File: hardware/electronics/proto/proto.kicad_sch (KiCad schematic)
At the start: 49 parts, among them J1 Conn_01x08_Female, U1 ADS131M06, U2 AP131-30

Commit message: Switch strain gauge footprints
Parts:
- R1, R10, R11, R12, R2, R3, R4, R5, R6, R7, R8, R9: value 1k -> 350; footprint Resistor_SMD:R_2512_6332Metric_Pad1.40x3.35mm_HandSolder -> proto:StrainGauge_BF350-3AA
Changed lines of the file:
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@@
       (effects (font (size 1.27 1.27)) (justify left))
     )
-    (property "Value" "1k" (id 1) (at 74.168 95.6822 0)
-      (effects (font (size 1.27 1.27)) (justify left))
-    )
-    (property "Footprint" "Resistor_SMD:R_2512_6332Metric_Pad1.40x3.35mm_HandSolder" (id 2) (at 70.612 93.98 90)
+    (property "Value" "350" (id 1) (at 74.168 95.6822 0)
+      (effects (font (size 1.27 1.27)) (justify left))
+    )
+    (property "Footprint" "proto:StrainGauge_BF350-3AA" (id 2) (at 70.612 93.98 90)
       (effects (font (size 1.27 1.27)) hide)
     )
@@
       (effects (font (size 1.27 1.27)) (justify left))
     )
-    (property "Value" "1k" (id 1) (at 61.468 85.5222 0)
-      (effects (font (size 1.27 1.27)) (justify left))
-    )
-    (property "Footprint" "Resistor_SMD:R_2512_6332Metric_Pad1.40x3.35mm_HandSolder" (id 2) (at 57.912 83.82 90)
+    (property "Value" "350" (id 1) (at 61.468 85.5222 0)
+      (effects (font (size 1.27 1.27)) (justify left))
+    )
+    (property "Footprint" "proto:StrainGauge_BF350-3AA" (id 2) (at 57.912 83.82 90)
       (effects (font (size 1.27 1.27)) hide)
     )
@@
       (effects (font (size 1.27 1.27)) (justify left))
     )
-    (property "Value" "1k" (id 1) (at 61.468 95.6822 0)
-      (effects (font (size 1.27 1.27)) (justify left))
-    )
-    (property "Footprint" "Resistor_SMD:R_2512_6332Metric_Pad1.40x3.35mm_HandSolder" (id 2) (at 57.912 93.98 90)
+    (property "Value" "350" (id 1) (at 61.468 95.6822 0)
+      (effects (font (size 1.27 1.27)) (justify left))
+    )
+    (property "Footprint" "proto:StrainGauge_BF350-3AA" (id 2) (at 57.912 93.98 90)
       (effects (font (size 1.27 1.27)) hide)
     )
@@
       (effects (font (size 1.27 1.27)) (justify left))
     )
-    (property "Value" "1k" (id 1) (at 36.068 85.5222 0)
-      (effects (font (size 1.27 1.27)) (justify left))
-    )
-    (property "Footprint" "Resistor_SMD:R_2512_6332Metric_Pad1.40x3.35mm_HandSolder" (id 2) (at 32.512 83.82 90)
+    (property "Value" "350" (id 1) (at 36.068 85.5222 0)
+      (effects (font (size 1.27 1.27)) (justify left))
+    )
+    (property "Footprint" "proto:StrainGauge_BF350-3AA" (id 2) (at 32.512 83.82 90)
       (effects (font (size 1.27 1.27)) hide)
     )
@@
       (effects (font (size 1.27 1.27)) (justify left))
     )
-    (property "Value" "1k" (id 1) (at 86.868 85.5222 0)
-      (effects (font (size 1.27 1.27)) (justify left))
-    )
-    (property "Footprint" "Resistor_SMD:R_2512_6332Metric_Pad1.40x3.35mm_HandSolder" (id 2) (at 83.312 83.82 90)
+    (property "Value" "350" (id 1) (at 86.868 85.5222 0)
+      (effects (font (size 1.27 1.27)) (justify left))
+    )
+    (property "Footprint" "proto:StrainGauge_BF350-3AA" (id 2) (at 83.312 83.82 90)
       (effects (font (size 1.27 1.27)) hide)
     )
@@
       (effects (font (size 1.27 1.27)) (justify left))
     )
-    (property "Value" "1k" (id 1) (at 36.068 95.6822 0)
-      (effects (font (size 1.27 1.27)) (justify left))
-    )
-    (property "Footprint" "Resistor_SMD:R_2512_6332Metric_Pad1.40x3.35mm_HandSolder" (id 2) (at 32.512 93.98 90)
+    (property "Value" "350" (id 1) (at 36.068 95.6822 0)
+      (effects (font (size 1.27 1.27)) (justify left))
+    )
+    (property "Footprint" "proto:StrainGauge_BF350-3AA" (id 2) (at 32.512 93.98 90)
       (effects (font (size 1.27 1.27)) hide)
     )
@@
       (effects (font (size 1.27 1.27)) (justify left))
     )
-    (property "Value" "1k" (id 1) (at 99.568 85.5222 0)
-      (effects (font (size 1.27 1.27)) (justify left))
-    )
-    (property "Footprint" "Resistor_SMD:R_2512_6332Metric_Pad1.40x3.35mm_HandSolder" (id 2) (at 96.012 83.82 90)
+    (property "Value" "350" (id 1) (at 99.568 85.5222 0)
+      (effects (font (size 1.27 1.27)) (justify left))
+    )
+    (property "Footprint" "proto:StrainGauge_BF350-3AA" (id 2) (at 96.012 83.82 90)
       (effects (font (size 1.27 1.27)) hide)
     )
@@
       (effects (font (size 1.27 1.27)) (justify left))
     )
-    (property "Value" "1k" (id 1) (at 48.768 95.6822 0)
-      (effects (font (size 1.27 1.27)) (justify left))
-    )
-    (property "Footprint" "Resistor_SMD:R_2512_6332Metric_Pad1.40x3.35mm_HandSolder" (id 2) (at 45.212 93.98 90)
+    (property "Value" "350" (id 1) (at 48.768 95.6822 0)
+      (effects (font (size 1.27 1.27)) (justify left))
+    )
+    (property "Footprint" "proto:StrainGauge_BF350-3AA" (id 2) (at 45.212 93.98 90)
       (effects (font (size 1.27 1.27)) hide)
     )
@@
       (effects (font (size 1.27 1.27)) (justify left))
     )
-    (property "Value" "1k" (id 1) (at 99.568 95.6822 0)
-      (effects (font (size 1.27 1.27)) (justify left))
-    )
-    (property "Footprint" "Resistor_SMD:R_2512_6332Metric_Pad1.40x3.35mm_HandSolder" (id 2) (at 96.012 93.98 90)
+    (property "Value" "350" (id 1) (at 99.568 95.6822 0)
+      (effects (font (size 1.27 1.27)) (justify left))
+    )
+    (property "Footprint" "proto:StrainGauge_BF350-3AA" (id 2) (at 96.012 93.98 90)
       (effects (font (size 1.27 1.27)) hide)
     )
@@
       (effects (font (size 1.27 1.27)) (justify left))
     )
-    (property "Value" "1k" (id 1) (at 74.168 85.5222 0)
-      (effects (font (size 1.27 1.27)) (justify left))
-    )
-    (property "Footprint" "Resistor_SMD:R_2512_6332Metric_Pad1.40x3.35mm_HandSolder" (id 2) (at 70.612 83.82 90)
+    (property "Value" "350" (id 1) (at 74.168 85.5222 0)
+      (effects (font (size 1.27 1.27)) (justify left))
+    )
+    (property "Footprint" "proto:StrainGauge_BF350-3AA" (id 2) (at 70.612 83.82 90)
       (effects (font (size 1.27 1.27)) hide)
     )
@@
       (effects (font (size 1.27 1.27)) (justify left))
     )
-    (property "Value" "1k" (id 1) (at 86.868 95.6822 0)
-      (effects (font (size 1.27 1.27)) (justify left))
-    )
-    (property "Footprint" "Resistor_SMD:R_2512_6332Metric_Pad1.40x3.35mm_HandSolder" (id 2) (at 83.312 93.98 90)
+    (property "Value" "350" (id 1) (at 86.868 95.6822 0)
+      (effects (font (size 1.27 1.27)) (justify left))
+    )
+    (property "Footprint" "proto:StrainGauge_BF350-3AA" (id 2) (at 83.312 93.98 90)
       (effects (font (size 1.27 1.27)) hide)
     )
@@
       (effects (font (size 1.27 1.27)) (justify left))
     )
-    (property "Value" "1k" (id 1) (at 48.768 85.5222 0)
-      (effects (font (size 1.27 1.27)) (justify left))
-    )
-    (property "Footprint" "Resistor_SMD:R_2512_6332Metric_Pad1.40x3.35mm_HandSolder" (id 2) (at 45.212 83.82 90)
+    (property "Value" "350" (id 1) (at 48.768 85.5222 0)
+      (effects (font (size 1.27 1.27)) (justify left))
+    )
+    (property "Footprint" "proto:StrainGauge_BF350-3AA" (id 2) (at 45.212 83.82 90)
       (effects (font (size 1.27 1.27)) hide)
     )
@@
     )
     (path "/41011989-3366-4344-ab51-8aa9fec0074e"
-      (reference "R1") (unit 1) (value "1k") (footprint "Resistor_SMD:R_2512_6332Metric_Pad1.40x3.35mm_HandSolder")
+      (reference "R1") (unit 1) (value "350") (footprint "proto:StrainGauge_BF350-3AA")
     )
     (path "/4e717e40-36ee-41e8-bf87-dae45943b227"
-      (reference "R2") (unit 1) (value "1k") (footprint "Resistor_SMD:R_2512_6332Metric_Pad1.40x3.35mm_HandSolder")
+      (reference "R2") (unit 1) (value "350") (footprint "proto:StrainGauge_BF350-3AA")
     )
     (path "/ec5aea88-77a2-47d1-bf87-700b2889e7bd"
-      (reference "R3") (unit 1) (value "1k") (footprint "Resistor_SMD:R_2512_6332Metric_Pad1.40x3.35mm_HandSolder")
+      (reference "R3") (unit 1) (value "350") (footprint "proto:StrainGauge_BF350-3AA")
     )
     (path "/aca853dc-1b03-4e20-af1f-8c7d54281a0a"
-      (reference "R4") (unit 1) (value "1k") (footprint "Resistor_SMD:R_2512_6332Metric_Pad1.40x3.35mm_HandSolder")
+      (reference "R4") (unit 1) (value "350") (footprint "proto:StrainGauge_BF350-3AA")
     )
     (path "/337ed533-99e7-4712-92e1-6da967478876"
-      (reference "R5") (unit 1) (value "1k") (footprint "Resistor_SMD:R_2512_6332Metric_Pad1.40x3.35mm_HandSolder")
+      (reference "R5") (unit 1) (value "350") (footprint "proto:StrainGauge_BF350-3AA")
     )
     (path "/36fdcefc-8eec-42a5-8d0d-8a934e0c7785"
-      (reference "R6") (unit 1) (value "1k") (footprint "Resistor_SMD:R_2512_6332Metric_Pad1.40x3.35mm_HandSolder")
+      (reference "R6") (unit 1) (value "350") (footprint "proto:StrainGauge_BF350-3AA")
     )
     (path "/cda38c69-f35f-4c61-912d-19c0526a4f60"
-      (reference "R7") (unit 1) (value "1k") (footprint "Resistor_SMD:R_2512_6332Metric_Pad1.40x3.35mm_HandSolder")
+      (reference "R7") (unit 1) (value "350") (footprint "proto:StrainGauge_BF350-3AA")
     )
     (path "/14436965-c74f-4397-8f25-61b4fa0f78ad"
-      (reference "R8") (unit 1) (value "1k") (footprint "Resistor_SMD:R_2512_6332Metric_Pad1.40x3.35mm_HandSolder")
+      (reference "R8") (unit 1) (value "350") (footprint "proto:StrainGauge_BF350-3AA")
     )
     (path "/478cb3c7-5e4c-44a6-835e-abd934c13f94"
-      (reference "R9") (unit 1) (value "1k") (footprint "Resistor_SMD:R_2512_6332Metric_Pad1.40x3.35mm_HandSolder")
+      (reference "R9") (unit 1) (value "350") (footprint "proto:StrainGauge_BF350-3AA")
     )
     (path "/da4d4a3f-b212-4225-bd5a-8fbd94b7afcc"
-      (reference "R10") (unit 1) (value "1k") (footprint "Resistor_SMD:R_2512_6332Metric_Pad1.40x3.35mm_HandSolder")
+      (reference "R10") (unit 1) (value "350") (footprint "proto:StrainGauge_BF350-3AA")
     )
     (path "/907dbaa3-9839-44c1-9c04-dcaf04ceafa3"
-      (reference "R11") (unit 1) (value "1k") (footprint "Resistor_SMD:R_2512_6332Metric_Pad1.40x3.35mm_HandSolder")
+      (reference "R11") (unit 1) (value "350") (footprint "proto:StrainGauge_BF350-3AA")
     )
     (path "/b349c835-8431-466a-bf34-d3c6228fb6ab"
-      (reference "R12") (unit 1) (value "1k") (footprint "Resistor_SMD:R_2512_6332Metric_Pad1.40x3.35mm_HandSolder")
+      (reference "R12") (unit 1) (value "350") (footprint "proto:StrainGauge_BF350-3AA")
     )
     (path "/a8676780-b6ab-4dec-89b6-29b8aa990012"

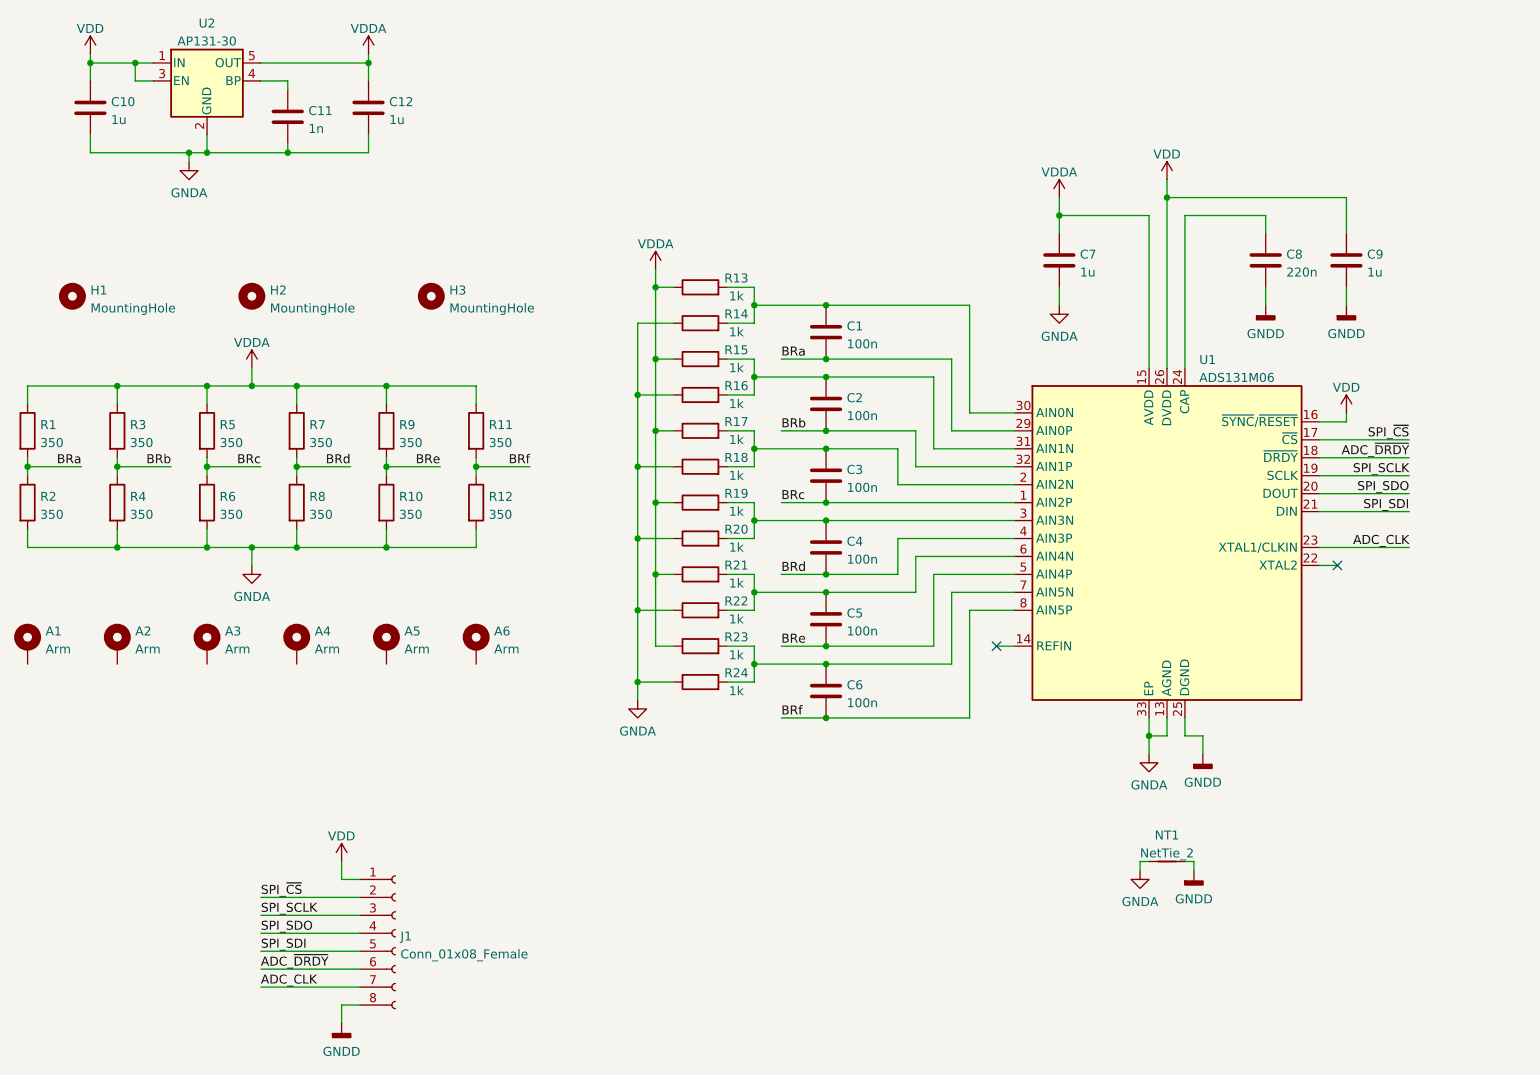
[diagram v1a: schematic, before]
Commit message: Update resistor values and add series R for better RC filtering
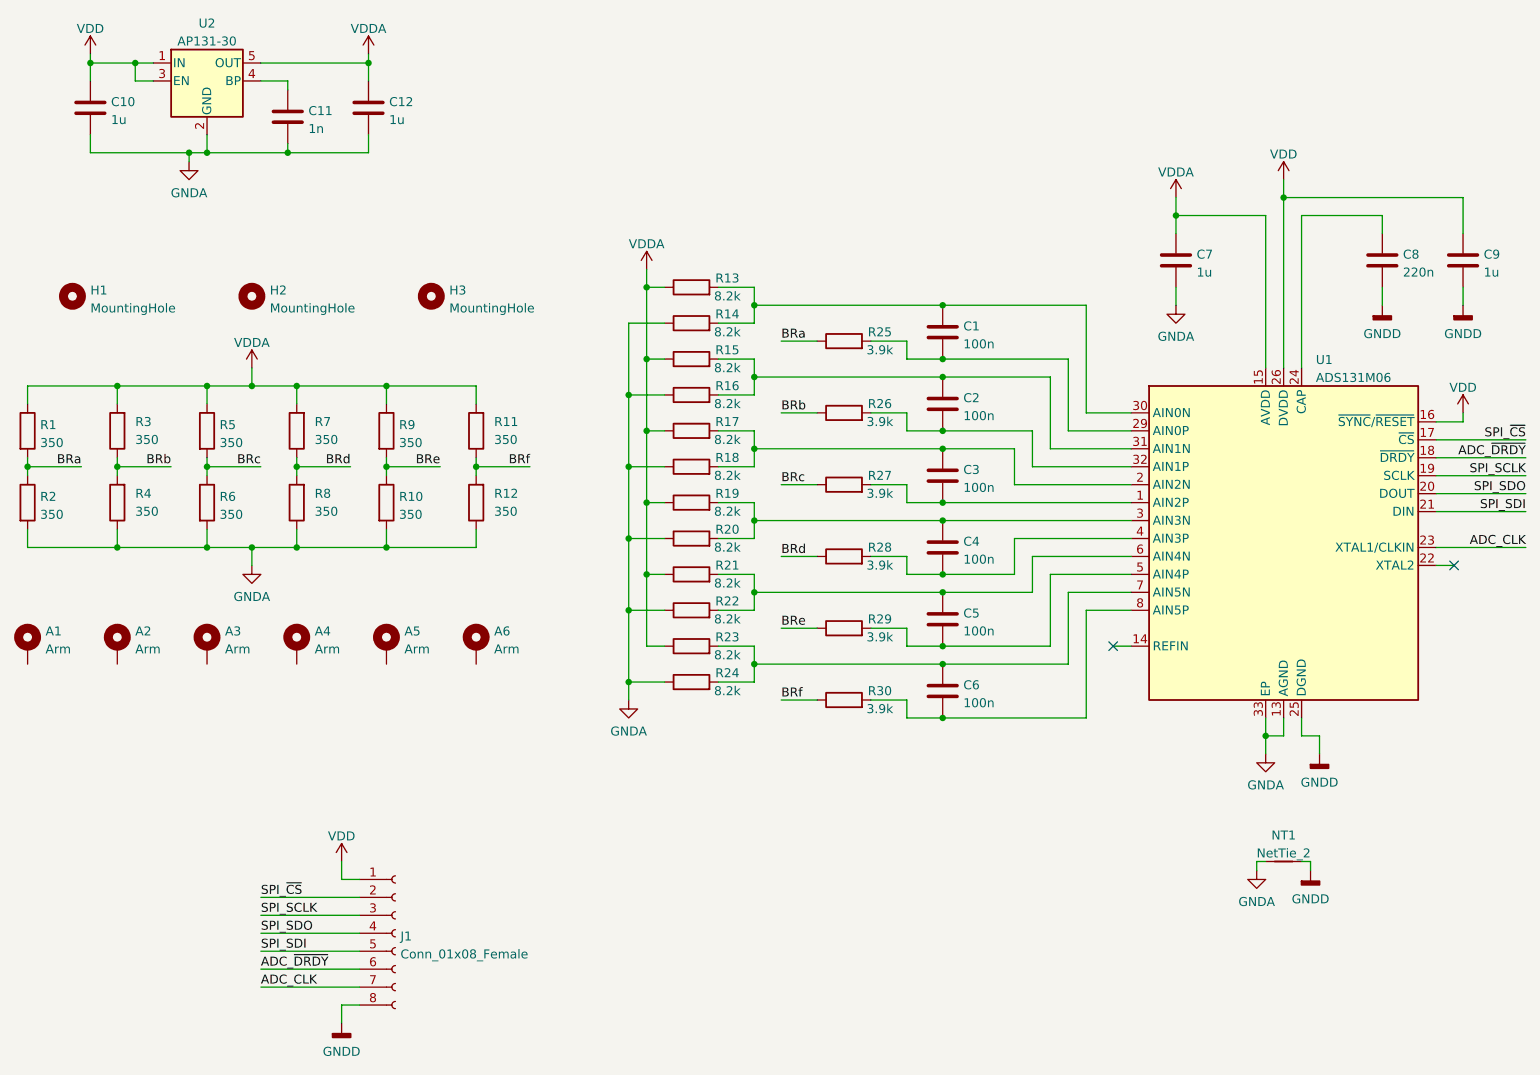
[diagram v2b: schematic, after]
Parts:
- added R25, R26, R27, R28, R29, R30: 3.9k, Resistor_SMD:R_0603_1608Metric_Pad0.98x0.95mm_HandSolder, symbol Device:R
- R13, R14, R15, R16, R17, R18, R19, R20, R21, R22, R23, R24: value 1k -> 8.2k
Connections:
- net BRa: now also R25.1; no longer C1.2, U1.29 (AIN0P)
- net BRb: now also R3.1, R4.2, R26.1; no longer C2.2, R3.2, R4.1, U1.32 (AIN1P)
- net BRc: now also R27.1; no longer C3.2, U1.1 (AIN2P)
- net BRd: now also R7.1, R8.2, R28.1; no longer C4.2, R7.2, R8.1, U1.4 (AIN3P)
- net BRe: now also R29.1; no longer C5.2, U1.5 (AIN4P)
- net BRf: now also R11.1, R12.2, R30.1; no longer C6.2, R11.2, R12.1, U1.8 (AIN5P)
- net GNDA: now also R12.1, R4.1, R8.1; no longer R12.2, R4.2, R8.2
- net VDDA: now also R11.2, R3.2, R7.2; no longer R11.1, R3.1, R7.1
- new net: C1.2, R25.2, U1.29 (AIN0P)
- new net: C6.2, R30.2, U1.8 (AIN5P)
- new net: C4.2, R28.2, U1.4 (AIN3P)
- new net: C2.2, R26.2, U1.32 (AIN1P)
- new net: C3.2, R27.2, U1.1 (AIN2P)
- new net: C5.2, R29.2, U1.5 (AIN4P)
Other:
- moved on the sheet: C1, C2, C3, C4, C5, C6, C7, C8, C9, NT1, R11, R12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

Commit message: Prepare for release of new prototype (#9)
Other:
- title: (none) -> Haptick Prototype Base
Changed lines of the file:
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@@
 (kicad_sch (version 20211123) (generator eeschema)
   (paper "A4")
+  (title_block
+    (title "Haptick Prototype Base")
+    (date "2023-01-13")
+    (rev "1.1.0")
+  )
   (junction (at 196.85 53.34) (diameter 0) (color 0 0 0 0)
   )

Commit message: Update manufacturers and part numbers for new prototype (#10)
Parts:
- R1, R10, R11, R12, R2, R3, R4, R5, R6, R7, R8, R9: Manufacturer TE Connectivity -> (none); Part Number CRGCQ2512F1K0 -> BF350-AA
- R13, R14, R15, R16, R17, R18, R19, R20, R21, R22, R23, R24: Part Number RT0603DRD071KL -> RT0603DRD078K2L
- R25, R26, R27, R28, R29, R30: Part Number RT0603DRD071KL -> RT0603DRD073K9L
